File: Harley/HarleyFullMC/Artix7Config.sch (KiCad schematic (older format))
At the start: 1 part, among them U1 xc7a50tcsg324pkg

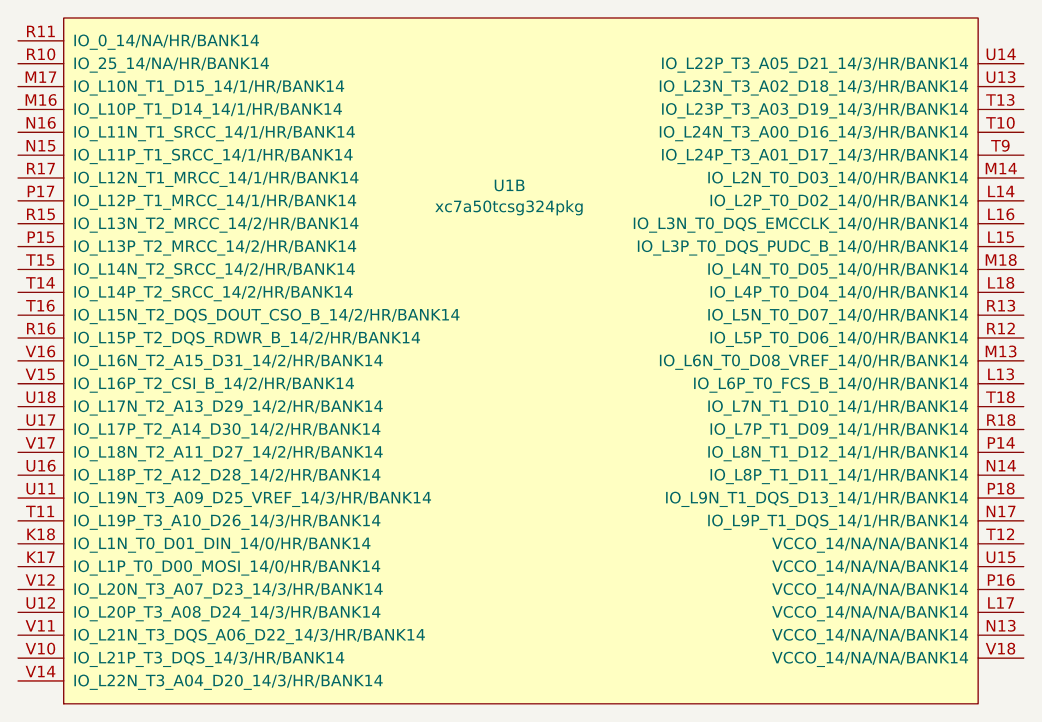
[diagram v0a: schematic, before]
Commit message: starting placing passives for HarleyFullMC
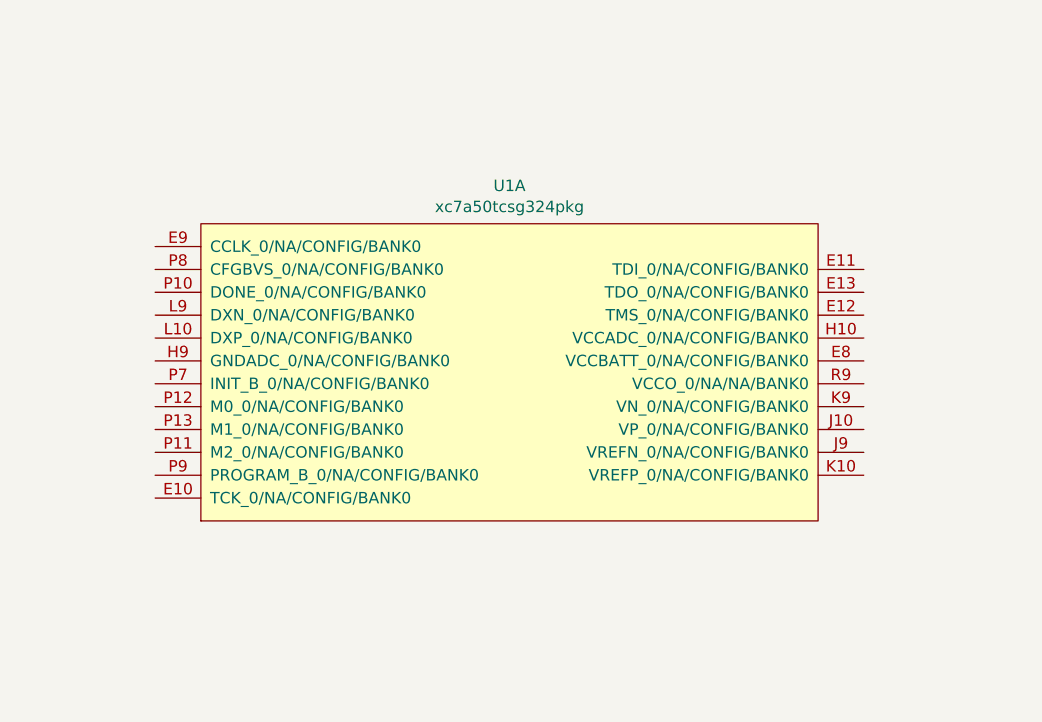
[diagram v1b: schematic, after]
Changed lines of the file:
@@
 EESchema Schematic File Version 2
+LIBS:artix7
+LIBS:cameras
+LIBS:DCDC_Converters
+LIBS:device
+LIBS:generic_ic
+LIBS:IMU
+LIBS:mt41k128m16
+LIBS:OSCILLATOR
+LIBS:usb3_connector
+LIBS:usb_controller
 LIBS:power
-LIBS:device
 LIBS:transistors
 LIBS:conn
@@
 LIBS:contrib
 LIBS:valves
-LIBS:DCDC_Converters
-LIBS:artix7
-LIBS:OSCILLATOR
-LIBS:mt41k128m16
-LIBS:HarleyProcessing-cache
+LIBS:HarleyFullMC-cache
 EELAYER 25 0
 EELAYER END
 $Descr A4 11693 8268
 encoding utf-8
-Sheet 2 10
+Sheet 4 14
 Title ""
 Date ""
@@
 $Comp
 L xc7a50tcsg324pkg U1
-U 2 1 56A03C5F
+U 1 1 56A03C5F
 P 3900 3750
 F 0 "U1" H 3850 4516 50  0000 C CNN
@@
 F 21 "_" H 3900 3750 50  0001 C CNN "Frequency"
 F 22 "_" H 3900 3750 50  0001 C CNN "ResonnanceFreq"
-	2    3900 3750
+	1    3900 3750
 	1    0    0    -1
 $EndComp

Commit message: start placing power supplies and power planes
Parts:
- added C118: 47u, Capacitors_SMD:C_0805, symbol C
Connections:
- net at U1.R9 (VCCO_0/NA/NA/BANK0): now also C118.1
- new net GND: C118.2
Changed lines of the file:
@@
+	1    0    0    -1
+$EndComp
+$Comp
+L C C118
+U 1 1 56A2EBA2
+P 6150 4000
+F 0 "C118" H 6200 4100 50  0000 L CNN
+F 1 "47u" H 6200 3900 50  0000 L CNN
+F 2 "Capacitors_SMD:C_0805" H 6188 3850 50  0001 C CNN
+F 3 "" H 6150 4000 50  0001 C CNN
+F 4 "_" H 6150 4000 50  0001 C CNN "MFN"
+F 5 "_" H 6150 4000 50  0001 C CNN "MFP"
+F 6 "digikey" H 6150 4000 50  0001 C CNN "D1"
+F 7 "mouser" H 6150 4000 50  0001 C CNN "D2"
+F 8 "_" H 6150 4000 50  0001 C CNN "D1PN"
+F 9 "_" H 6150 4000 50  0001 C CNN "D1PL"
+F 10 "_" H 6150 4000 50  0001 C CNN "D2PN"
+F 11 "_" H 6150 4000 50  0001 C CNN "D2PL"
+F 12 "0402" H 6150 4000 50  0001 C CNN "Package"
+F 13 "_" H 6265 3908 50  0001 L CNN "Description"
+F 14 "6.3" H 6150 4000 50  0001 C CNN "Voltage"
+F 15 "_" H 6150 4000 50  0001 C CNN "Power"
+F 16 "10%" H 6150 4000 50  0001 C CNN "Tolerance"
+F 17 "X5R" H 6150 4000 50  0001 C CNN "Temperature"
+F 18 "_" H 6150 4000 50  0001 C CNN "ReverseVoltage"
+F 19 "_" H 6150 4000 50  0001 C CNN "ForwardVoltage"
+F 20 "_" H 6150 4000 50  0001 C CNN "Cont.Current"
+F 21 "_" H 6150 4000 50  0001 C CNN "Frequency"
+F 22 "_" H 6150 4000 50  0001 C CNN "ResonnanceFreq"
+	1    6150 4000
+	1    0    0    -1
+$EndComp
+Wire Wire Line
+	5400 3850 6150 3850
+$Comp
+L GND #PWR75
+U 1 1 56A2EBB3
+P 6150 4150
+F 0 "#PWR75" H 6150 3900 50  0001 C CNN
+F 1 "GND" H 6158 3976 50  0000 C CNN
+F 2 "" H 6150 4150 50  0000 C CNN
+F 3 "" H 6150 4150 50  0000 C CNN
+	1    6150 4150
 	1    0    0    -1
 $EndComp

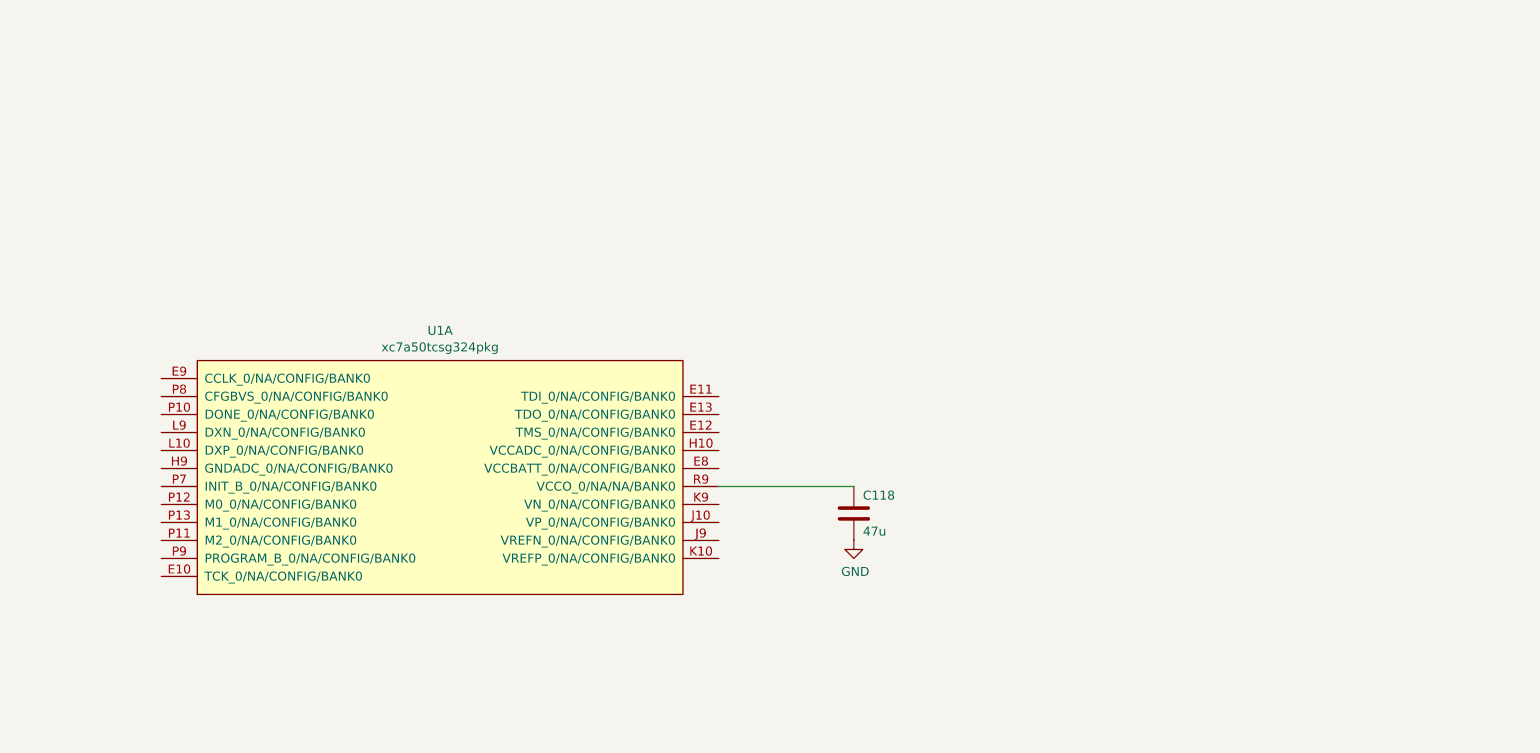
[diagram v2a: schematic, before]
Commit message: finished placement and started routing
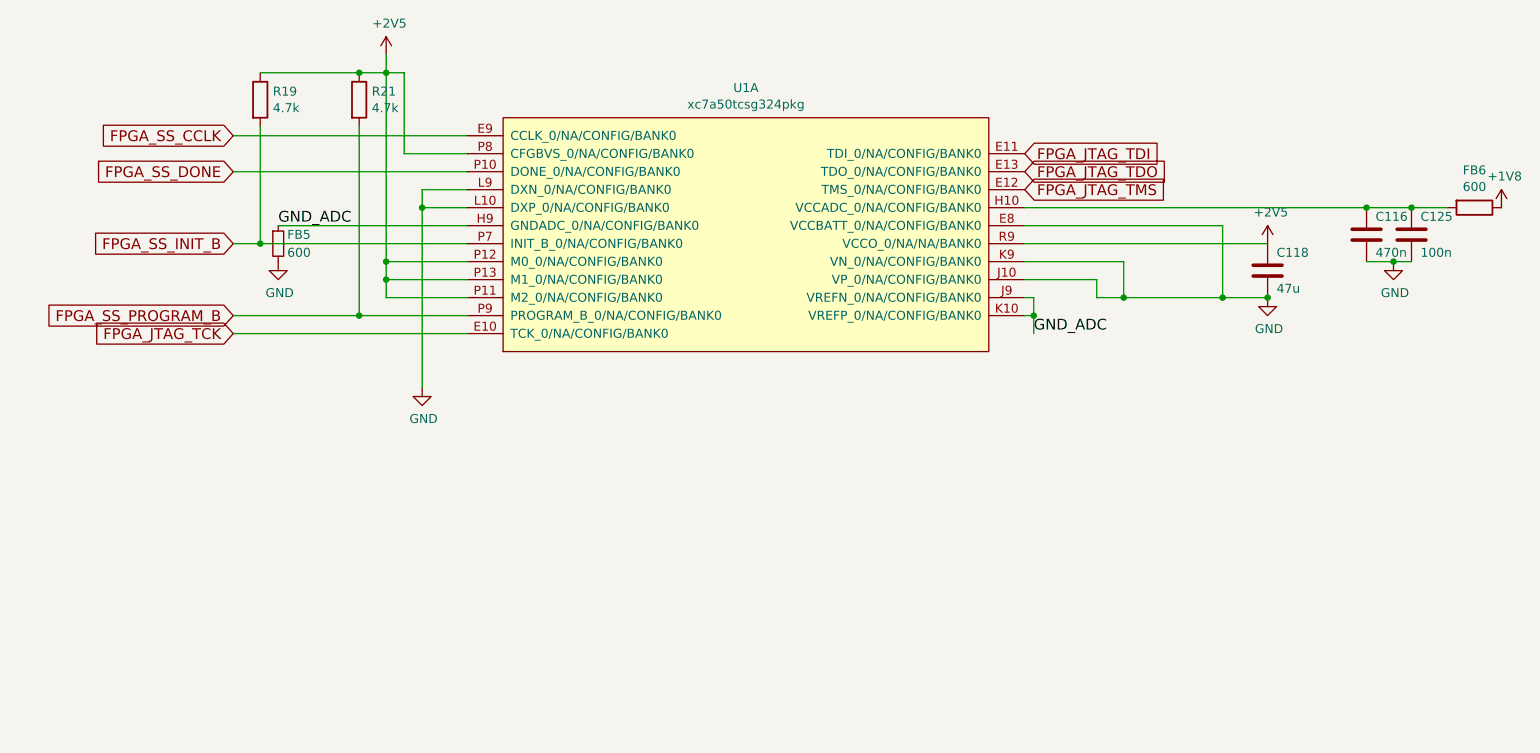
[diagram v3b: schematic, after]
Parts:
- added C116: 470n, Dipoles_SMD:C_0201, symbol C
- added C125: 100n, Dipoles_SMD:C_0201, symbol C
- added FB5: 600, Dipoles_SMD:C_0201, symbol R_Small
- added FB6: 600, Dipoles_SMD:C_0201, symbol R
- added R19, R21: 4.7k, Dipoles_SMD:C_0201, symbol R
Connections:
- net GND: now also U1.E8 (VCCBATT_0/NA/CONFIG/BANK0), U1.J10 (VP_0/NA/CONFIG/BANK0), U1.K9 (VN_0/NA/CONFIG/BANK0), U1.L10 (DXP_0/NA/CONFIG/BANK0), U1.L9 (DXN_0/NA/CONFIG/BANK0), C116.2, C125.2, FB5.2
- net FPGA_JTAG_TCK: now reaches U1.E10 (TCK_0/NA/CONFIG/BANK0)
- net FPGA_JTAG_TDI: now reaches U1.E11 (TDI_0/NA/CONFIG/BANK0)
- net FPGA_JTAG_TMS: now reaches U1.E12 (TMS_0/NA/CONFIG/BANK0)
- net FPGA_JTAG_TDO: now reaches U1.E13 (TDO_0/NA/CONFIG/BANK0)
- net FPGA_SS_CCLK: now reaches U1.E9 (CCLK_0/NA/CONFIG/BANK0)
- net at U1.H10 (VCCADC_0/NA/CONFIG/BANK0): now also C116.1, C125.1, FB6.2
- net GND_ADC: now reaches U1.H9 (GNDADC_0/NA/CONFIG/BANK0)
- net GND_ADC: now also U1.J9 (VREFN_0/NA/CONFIG/BANK0), U1.K10 (VREFP_0/NA/CONFIG/BANK0), FB5.1
- net FPGA_SS_DONE: now reaches U1.P10 (DONE_0/NA/CONFIG/BANK0)
- net +2V5: now reaches U1.P11 (M2_0/NA/CONFIG/BANK0)
- net +2V5: now also C118.1, U1.P12 (M0_0/NA/CONFIG/BANK0), U1.P13 (M1_0/NA/CONFIG/BANK0), U1.P8 (CFGBVS_0/NA/CONFIG/BANK0), U1.R9 (VCCO_0/NA/NA/BANK0), R19.1, R21.1
- net FPGA_SS_INIT_B: now reaches U1.P7 (INIT_B_0/NA/CONFIG/BANK0)
- net FPGA_SS_INIT_B: now also R19.2
- net FPGA_SS_PROGRAM_B: now reaches U1.P9 (PROGRAM_B_0/NA/CONFIG/BANK0)
- net FPGA_SS_PROGRAM_B: now also R21.2
- new net +1V8: FB6.1
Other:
- moved on the sheet: C118, U1A

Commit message: generate BOM and update all components accordingly
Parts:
- C116: D1PL _ -> http://www.digikey.com/product-detail/en/C0603X5R0J474K030B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; D1PN _ -> 445-13653; MFN _ -> TDK; MFP _ -> C0603X5R0J474K030BC; Package 0402 -> 0201
- C118: D1PL _ -> http://www.digikey.com/product-detail/en/C2012X5R1A476M125A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; D1PN _ -> 445-8239; MFN _ -> TDK; MFP _ -> C2012X5R1A476M125AC; Package 0402 -> 0805; Tolerance 10% -> 20%; Voltage 6.3 -> 10
- C125: D1PL _ -> http://www.digikey.com/product-detail/en/C1005X5R0J104K050B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; D1PN _ -> 445-1266; MFN _ -> TDK; MFP _ -> C1005X5R0J104K050BA
- FB5, FB6: D1PL _ -> http://www.digikey.com/product-detail/en/BK0603TM601-T/587-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; D1PN _ -> 587-3273; MFN _ -> Taiyo Yuden; MFP _ -> BK0603TM601; Package 0402 -> 0201; Power 1/16 -> _; Tolerance 1% -> _
- R19, R21: D1PL _ -> http://www.digikey.com/product-detail/en/CRCW02014K70FKED/5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; D1PN _ -> 541-4.70KAAB; MFN _ -> Vishay; MFP _ -> CRCW02016K7FKED; Power 1/16 -> 1/20
- U1: D1 digikey -> avnet; D1PL _ -> http://avnetexpress.avnet.com/store/em/EMController?action=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; D1PN _ -> XC7A50T-2CSG324C; D2 mouser -> _; MFN _ -> Xilinx; MFP _ -> XC7A50T-2CSG324C
